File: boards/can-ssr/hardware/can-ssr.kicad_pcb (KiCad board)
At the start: 2 copper layers, 100 x 100 mm, 127 parts, among them J1 CAN IN, J2 CAN OUT, J3 ICSP, J30 MEAN WELL, J4 UART, Q1 IPB110N20N3LF, Q2 IPB110N20N3LF, Q20 2N7002, Q21 2N7002, Q22 2N7002, Q23 2N7002, Q24 2N7002, Q3 IPB110N20N3LF, Q4 IPB110N20N3LF, Q5 MMBT2907A, SW1 ADDR, U1 R-78E5.0-1.0, U10 VOM1271T, U11 VOM1271T, U12 ACS770ECB-100U-PFF-T, U2 MCP2562FD-E/P, U20 LM393B, U3 PIC18F47Q84-I/PT, U30 UCC12050DVE, U31 ISO1640DWR, U32 MCP3426A0-E/SN, U33 MCP4725A0T-E/CH, U34 MCP4725A0T-E/CH, U35 TLP222A, U36 MCP3426A1-E/SN, U40 MAX7219CWG+, U41 CC56-12SRWA, Y1 16MHz

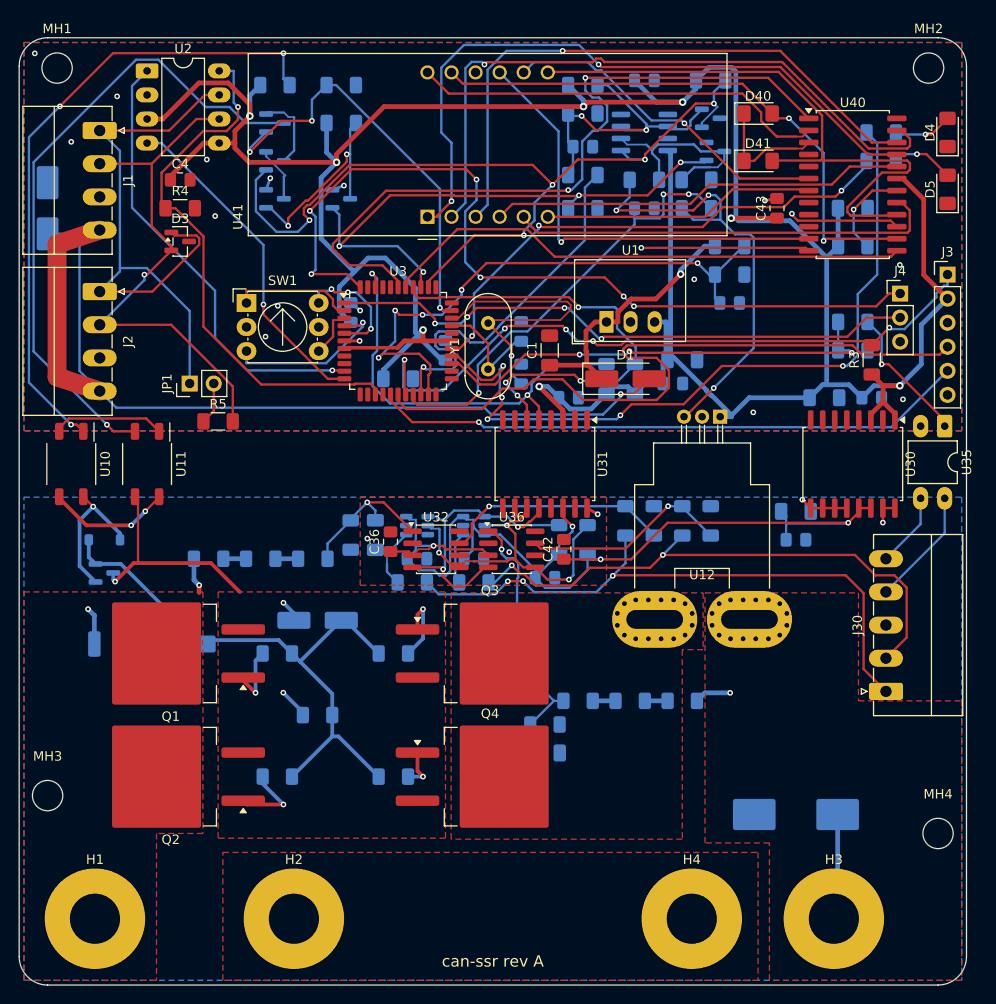
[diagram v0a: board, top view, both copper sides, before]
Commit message: can-ssr: re-route with bottom as ground plane (13 connections open)
- Logic bottom-side passives moved to the top next to their ICs; only the
  trip / LED-drive cluster stays on the bottom, under the display
- Ground first: every top-side GND / GND_LOAD SMD pad gets a stub and via
  to the bottom plane before signal routing
- Signals autorouted with the bottom restricted to the under-display
  block, the PIC escape area, the ADC/DAC band and small hop windows;
  gate-drive / HV routing unchanged
- Island bridges and stitching; 2 mm V12_BUS pass-through on the bottom
- DRC: no clearance or short violations. Open: 13 connections
- .gitignore: KiCad 10 .history/ folders

Co-Authored-By: Claude Opus 5.5 <noreply@anthropic.com>
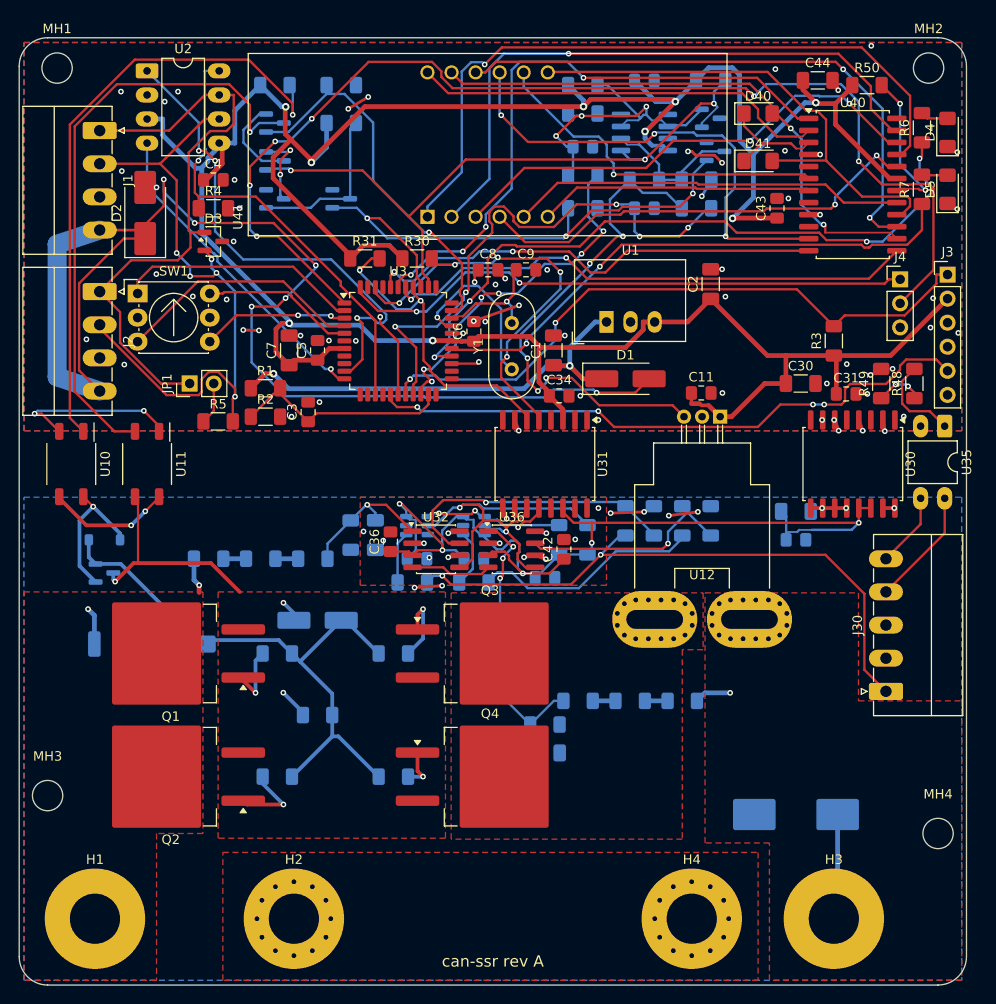
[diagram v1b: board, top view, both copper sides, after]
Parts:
- C11, C2, C3, C30, C31, C34, C44, C5, C6, C7, C8, C9, D2, R1, R2, R30, R31, R48, R49, R50, R6, R7: moved to F.Cu
- moved R1 51.2 mm to (126.0, 137.0)
- moved R2 51.2 mm to (126.0, 140.0)
- moved C3 46.0 mm to (130.5, 139.5), turned to 90 degrees
- moved R31 31.2 mm to (136.5, 123.3), turned to 0 degrees
- moved R30 23.7 mm to (142.0, 123.3), turned to 0 degrees
- moved R50 17.1 mm to (189.5, 105.0)
- moved C44 14.0 mm to (184.3, 104.5)
- moved C7 11.9 mm to (128.5, 133.0), turned to 90 degrees
- moved SW1 11.5 mm to (112.5, 127.0)
- moved C9 11.0 mm to (153.5, 124.5), turned to 0 degrees
- moved D2 10.3 mm to (113.3, 118.5)
- moved R48 9.19 mm to (194.5, 136.5), turned to 90 degrees
- moved C2 8.54 mm to (173.0, 126.0), turned to 90 degrees
- moved C8 7.38 mm to (149.5, 124.5), turned to 0 degrees
- moved C5 5.32 mm to (131.5, 133.0)
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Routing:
- net /CAN, power, MCU/ICSPDAT: track 75.3 -> 8.98 mm, vias 0 -> 1
- net /CAN, power, MCU/UART_RX: track 62.8 -> 120.8 mm, vias 4 -> 6
- net /Display/SEG_F: track 11.7 -> 60.8 mm, vias 1 -> 2
- net MW_REMOTE: track 49.2 -> 7.98 mm
- net /CAN, power, MCU/V12_MON: track 59.8 -> 23.4 mm, vias 5 -> 0
- net /Load-side sense and supply control/MW_PC: track 59.8 -> 24.1 mm, vias 2 -> 0
- net DISP_LOAD: track 17.8 -> 49.1 mm, vias 1 -> 2
- net /CAN, power, MCU/V12_BUS: track 107.6 -> 138.3 mm, vias 1 -> 6
- net /CAN, power, MCU/UART_TX: track 90.3 -> 60.8 mm, vias 6 -> 2
- net +12V: track 27.9 -> 48.6 mm, vias 1 -> 2
- net TRIP_OK: track 91.8 -> 71.9 mm, vias 5 -> 3
- net GND: track 6.80 -> 26.2 mm, vias 16 -> 62
- net /CAN, power, MCU/OSC2: track 31.3 -> 12.8 mm
- net I2C_SCL: track 49.4 -> 33.5 mm, vias 4 -> 2
- net /CAN, power, MCU/CANL: track 56.2 -> 71.1 mm, vias 1 -> 5
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
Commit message: can-ssr: drop top ground pours, solid bottom pours (6 connections open)
- Removed the top-layer GND and GND_LOAD signal pours; ground is the
  bottom plane only. RET top (load-return copper) and power pours kept
- GND bottom and RET bottom connect pads solid (no thermal relief)
- Top stubs from ground pads to their vias, grid-routed ground island
  links, +5V at U30, ICSPDAT, MW_PC; SDA_ISO track ends fixed
- Removed 21 dangling ground stitching vias
- DRC: no errors. Open: MW_REMOTE (U3.25-R49) and five small
  bottom-plane islands (C8.2, U20.4/R21.2, U20.5, U32.8/U34.2, C35.2)

Co-Authored-By: Claude Opus 5.5 <noreply@anthropic.com>
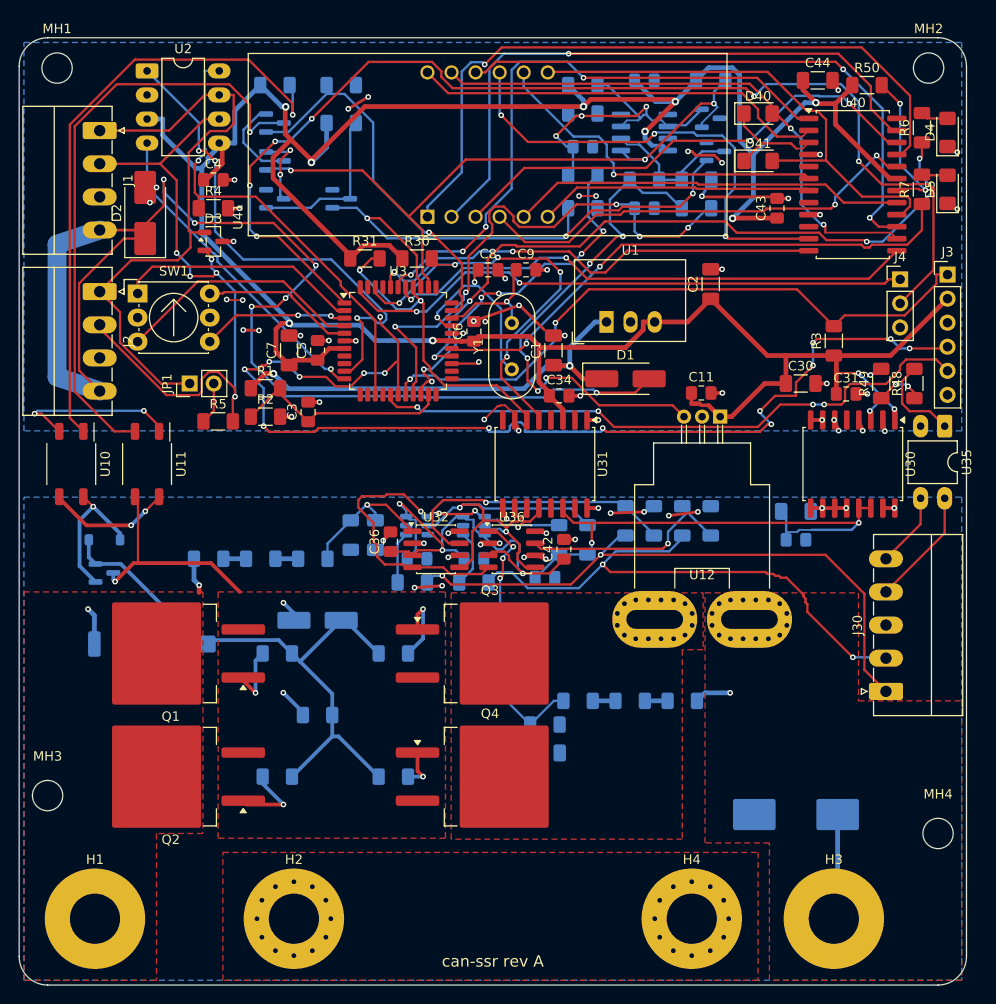
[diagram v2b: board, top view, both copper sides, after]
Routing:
- net /CAN, power, MCU/ICSPDAT: track 8.98 -> 117.6 mm, vias 1 -> 15
- net GND: track 26.2 -> 63.2 mm, vias 62 -> 48
- net /Load-side sense and supply control/MW_PC: track 24.1 -> 57.0 mm, vias 0 -> 2
- net /Load-side sense and supply control/SDA_ISO: track 26.9 -> 45.8 mm, vias 3 -> 4
- net +5V: track 320.5 -> 330.0 mm, vias 9 -> 12
- net GND_LOAD: track 22.0 -> 25.6 mm, vias 46 -> 45
- removed copper zone on F.Cu, net GND
